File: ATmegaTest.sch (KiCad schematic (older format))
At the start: 13 parts, among them P1 Digital, P10 CONN_01X01, P11 CONN_01X01, P12 CONN_01X01, P13 CONN_01X01, P2 Power, P3 Analog, P4 Analog, P5 PWM, P6 PWM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

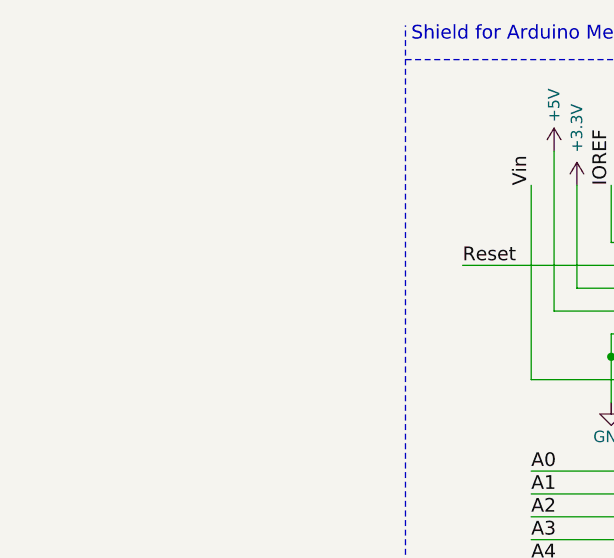
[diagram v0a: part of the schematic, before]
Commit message: RESET ckt
reset circuit for uC
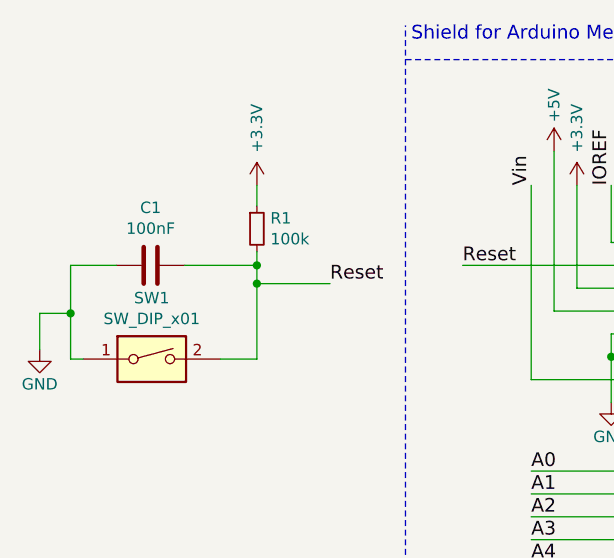
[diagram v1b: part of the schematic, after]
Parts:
- added C1: 100nF, Capacitor_SMD:C_0603_1608Metric, symbol Device:C
- added R1: 100k, Resistor_SMD:R_0603_1608Metric, symbol Device:R_Small
- added SW1: SW_DIP_x01, Button_Switch_SMD:SW_SPST_CK_KXT3, symbol Switch:SW_DIP_x01
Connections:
- net +3V3: now also R1.1
- net GND: now also C1.2, SW1.1
- net Reset: now also C1.1, R1.2, SW1.2
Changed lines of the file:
@@
 Wire Notes Line
 	8350 6050 8350 500
+$Comp
+L Switch:SW_DIP_x01 SW1
+U 1 1 5DB39D7E
+P 7240 1960
+F 0 "SW1" H 7240 2227 50  0000 C CNN
+F 1 "SW_DIP_x01" H 7240 2136 50  0000 C CNN
+F 2 "Button_Switch_SMD:SW_SPST_CK_KXT3" H 7240 1960 50  0001 C CNN
+F 3 "~" H 7240 1960 50  0001 C CNN
+	1    7240 1960
+	1    0    0    -1
+$EndComp
+$Comp
+L Device:C C1
+U 1 1 5DB435FB
+P 7235 1550
+F 0 "C1" V 6983 1550 50  0000 C CNN
+F 1 "100nF" V 7074 1550 50  0000 C CNN
+F 2 "Capacitor_SMD:C_0603_1608Metric" H 7273 1400 50  0001 C CNN
+F 3 "~" H 7235 1550 50  0001 C CNN
+	1    7235 1550
+	0    1    1    0
+$EndComp
+$Comp
+L Device:R_Small R1
+U 1 1 5DB43DF8
+P 7700 1390
+F 0 "R1" H 7759 1436 50  0000 L CNN
+F 1 "100k" H 7759 1345 50  0000 L CNN
+F 2 "Resistor_SMD:R_0603_1608Metric" H 7700 1390 50  0001 C CNN
+F 3 "~" H 7700 1390 50  0001 C CNN
+	1    7700 1390
+	1    0    0    -1
+$EndComp
+Wire Wire Line
+	7700 1200 7700 1290
+Wire Wire Line
+	7700 1490 7700 1550
+Wire Wire Line
+	7700 1960 7540 1960
+Wire Wire Line
+	7385 1550 7700 1550
+Connection ~ 7700 1550
+Wire Wire Line
+	7700 1550 7700 1630
+Wire Wire Line
+	7085 1550 6885 1550
+Wire Wire Line
+	6885 1550 6885 1760
+Wire Wire Line
+	6885 1960 6940 1960
+Wire Wire Line
+	6750 1920 6750 1760
+Wire Wire Line
+	6750 1760 6885 1760
+Connection ~ 6885 1760
+Wire Wire Line
+	6885 1760 6885 1960
+$Comp
+L power:+3V3 #PWR08
+U 1 1 5DB6ABCB
+P 7700 1200
+F 0 "#PWR08" H 7700 1050 50  0001 C CNN
+F 1 "+3.3V" V 7700 1450 50  0000 C CNN
+F 2 "" H 7700 1200 50  0000 C CNN
+F 3 "" H 7700 1200 50  0000 C CNN
+	1    7700 1200
+	1    0    0    -1
+$EndComp
+Wire Wire Line
+	7700 1630 8020 1630
+Connection ~ 7700 1630
+Wire Wire Line
+	7700 1630 7700 1960
+Text Label 8020 1630 0    60   ~ 0
+Reset
+$Comp
+L power:GND #PWR?
+U 1 1 5DB848D9
+P 6750 1920
+F 0 "#PWR?" H 6750 1670 50  0001 C CNN
+F 1 "GND" H 6750 1770 50  0000 C CNN
+F 2 "" H 6750 1920 50  0000 C CNN
+F 3 "" H 6750 1920 50  0000 C CNN
+	1    6750 1920
+	1    0    0    -1
+$EndComp
 $EndSCHEMATC

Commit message: Update ATmegaTest.sch
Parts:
- SW1: footprint Button_Switch_SMD:SW_SPST_CK_KXT3 -> (none)
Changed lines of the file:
@@
 F 0 "SW1" H 7240 2227 50  0000 C CNN
 F 1 "SW_DIP_x01" H 7240 2136 50  0000 C CNN
-F 2 "Button_Switch_SMD:SW_SPST_CK_KXT3" H 7240 1960 50  0001 C CNN
+F 2 "" H 7240 1960 50  0001 C CNN
 F 3 "~" H 7240 1960 50  0001 C CNN
 	1    7240 1960
@@
 Reset
 $Comp
-L power:GND #PWR?
+L power:GND #PWR0101
 U 1 1 5DB848D9
 P 6750 1920
-F 0 "#PWR?" H 6750 1670 50  0001 C CNN
+F 0 "#PWR0101" H 6750 1670 50  0001 C CNN
 F 1 "GND" H 6750 1770 50  0000 C CNN
 F 2 "" H 6750 1920 50  0000 C CNN

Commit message: DividerCkt
Voltage Divider with analogInput  to ATMEGA
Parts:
- added R? (x2): 10k, Resistor_SMD:R_0603_1608Metric, symbol Device:R_Small
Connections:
- net +3V3: now also R?.1
- net A0: now also R?.1, R?.2
- net GND: now also R?.2
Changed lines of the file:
@@
 EESchema Schematic File Version 4
-LIBS:ATmegaTest-cache
 EELAYER 29 0
 EELAYER END
@@
 P 9950 1550
 F 0 "P5" H 9950 2050 50  0000 C CNN
-F 1 "PWM" V 10050 1550 50  0000 C CNN
+F 1 "PWM" V 10050 1550 50  0000 C CNB
 F 2 "Socket_Arduino_Mega:Socket_Strip_Arduino_1x10" H 9950 1550 50  0001 C CNN
 F 3 "" H 9950 1550 50  0000 C CNN
@@
 	1    0    0    -1
 $EndComp
+$Comp
+L power:+3V3 #PWR?
+U 1 1 5DB90B5B
+P 6260 935
+F 0 "#PWR?" H 6260 785 50  0001 C CNN
+F 1 "+3.3V" V 6260 1185 50  0000 C CNN
+F 2 "" H 6260 935 50  0000 C CNN
+F 3 "" H 6260 935 50  0000 C CNN
+	1    6260 935
+	1    0    0    -1
+$EndComp
+$Comp
+L Device:R_Small R?
+U 1 1 5DB97808
+P 6260 1145
+F 0 "R?" H 6319 1191 50  0000 L CNN
+F 1 "10k" H 6319 1100 50  0000 L CNN
+F 2 "Resistor_SMD:R_0603_1608Metric" H 6260 1145 50  0001 C CNN
+F 3 "~" H 6260 1145 50  0001 C CNN
+	1    6260 1145
+	1    0    0    -1
+$EndComp
+Wire Wire Line
+	6260 1245 6260 1305
+Wire Wire Line
+	6260 1045 6260 935
+Wire Wire Line
+	6260 1760 6750 1760
+Connection ~ 6750 1760
+$Comp
+L Device:R_Small R?
+U 1 1 5DBA2C8F
+P 6260 1465
+F 0 "R?" H 6319 1511 50  0000 L CNN
+F 1 "10k" H 6319 1420 50  0000 L CNN
+F 2 "Resistor_SMD:R_0603_1608Metric" H 6260 1465 50  0001 C CNN
+F 3 "~" H 6260 1465 50  0001 C CNN
+	1    6260 1465
+	1    0    0    -1
+$EndComp
+Wire Wire Line
+	6260 1565 6260 1760
+Wire Wire Line
+	6260 1305 6560 1305
+Connection ~ 6260 1305
+Wire Wire Line
+	6260 1305 6260 1365
+Text Label 6560 1305 0    50   ~ 0
+A0
 $EndSCHEMATC

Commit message: Revert "DividerCkt"
This reverts commit 058e6e4fb967e27780ca64c39ae31b78ca90827e.
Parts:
- removed R? (x2): 10k, Resistor_SMD:R_0603_1608Metric, symbol Device:R_Small
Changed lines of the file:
@@
 EESchema Schematic File Version 4
+LIBS:ATmegaTest-cache
 EELAYER 29 0
 EELAYER END
@@
 P 9950 1550
 F 0 "P5" H 9950 2050 50  0000 C CNN
-F 1 "PWM" V 10050 1550 50  0000 C CNB
+F 1 "PWM" V 10050 1550 50  0000 C CNN
 F 2 "Socket_Arduino_Mega:Socket_Strip_Arduino_1x10" H 9950 1550 50  0001 C CNN
 F 3 "" H 9950 1550 50  0000 C CNN
@@
 	1    0    0    -1
 $EndComp
-$Comp
-L power:+3V3 #PWR?
-U 1 1 5DB90B5B
-P 6260 935
-F 0 "#PWR?" H 6260 785 50  0001 C CNN
-F 1 "+3.3V" V 6260 1185 50  0000 C CNN
-F 2 "" H 6260 935 50  0000 C CNN
-F 3 "" H 6260 935 50  0000 C CNN
-	1    6260 935
-	1    0    0    -1
-$EndComp
-$Comp
-L Device:R_Small R?
-U 1 1 5DB97808
-P 6260 1145
-F 0 "R?" H 6319 1191 50  0000 L CNN
-F 1 "10k" H 6319 1100 50  0000 L CNN
-F 2 "Resistor_SMD:R_0603_1608Metric" H 6260 1145 50  0001 C CNN
-F 3 "~" H 6260 1145 50  0001 C CNN
-	1    6260 1145
-	1    0    0    -1
-$EndComp
-Wire Wire Line
-	6260 1245 6260 1305
-Wire Wire Line
-	6260 1045 6260 935
-Wire Wire Line
-	6260 1760 6750 1760
-Connection ~ 6750 1760
-$Comp
-L Device:R_Small R?
-U 1 1 5DBA2C8F
-P 6260 1465
-F 0 "R?" H 6319 1511 50  0000 L CNN
-F 1 "10k" H 6319 1420 50  0000 L CNN
-F 2 "Resistor_SMD:R_0603_1608Metric" H 6260 1465 50  0001 C CNN
-F 3 "~" H 6260 1465 50  0001 C CNN
-	1    6260 1465
-	1    0    0    -1
-$EndComp
-Wire Wire Line
-	6260 1565 6260 1760
-Wire Wire Line
-	6260 1305 6560 1305
-Connection ~ 6260 1305
-Wire Wire Line
-	6260 1305 6260 1365
-Text Label 6560 1305 0    50   ~ 0
-A0
 $EndSCHEMATC
